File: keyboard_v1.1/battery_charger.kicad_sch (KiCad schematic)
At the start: 40 parts, among them Q3 AO3400A, Q4 AO3400A, SW13 25336NA, U1 max1737eei+T

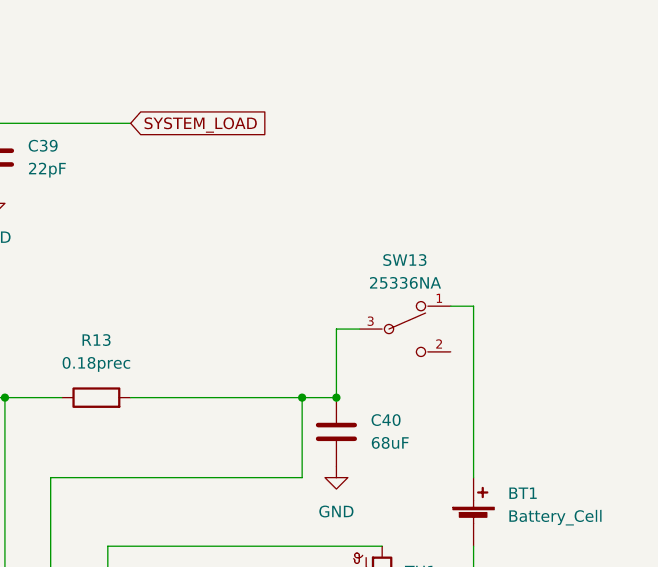
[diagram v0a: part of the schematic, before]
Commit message: 2022-04-14 added vias and led positions
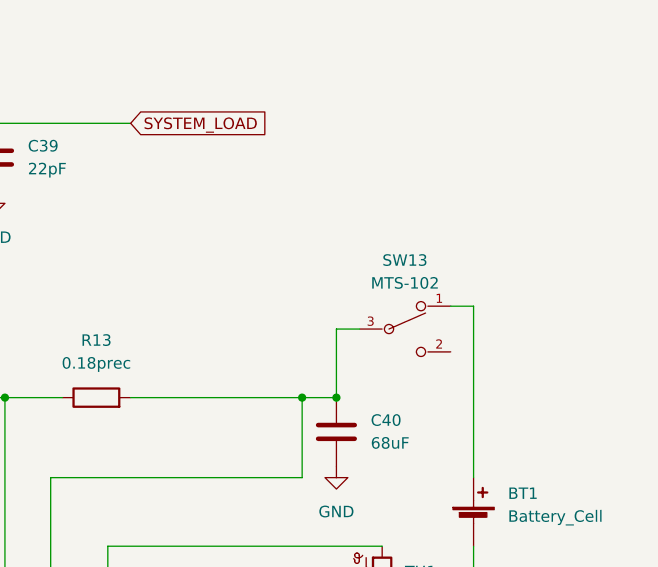
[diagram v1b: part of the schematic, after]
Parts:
- SW13: value 25336NA -> MTS-102
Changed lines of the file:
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@@
     (in_bom yes) (on_board yes) (fields_autoplaced)
     (property "Reference" "SW13" (id 0) (at 270.51 102.87 0))
-    (property "Value" "25336NA" (id 1) (at 270.51 105.41 0))
+    (property "Value" "MTS-102" (id 1) (at 270.51 105.41 0))
     (property "Footprint" "Switch_ApemInc:Apem_Inc.-25336NA-MFG" (id 2) (at 262.89 97.79 0)
       (effects (font (size 1.27 1.27)) (justify left) hide)

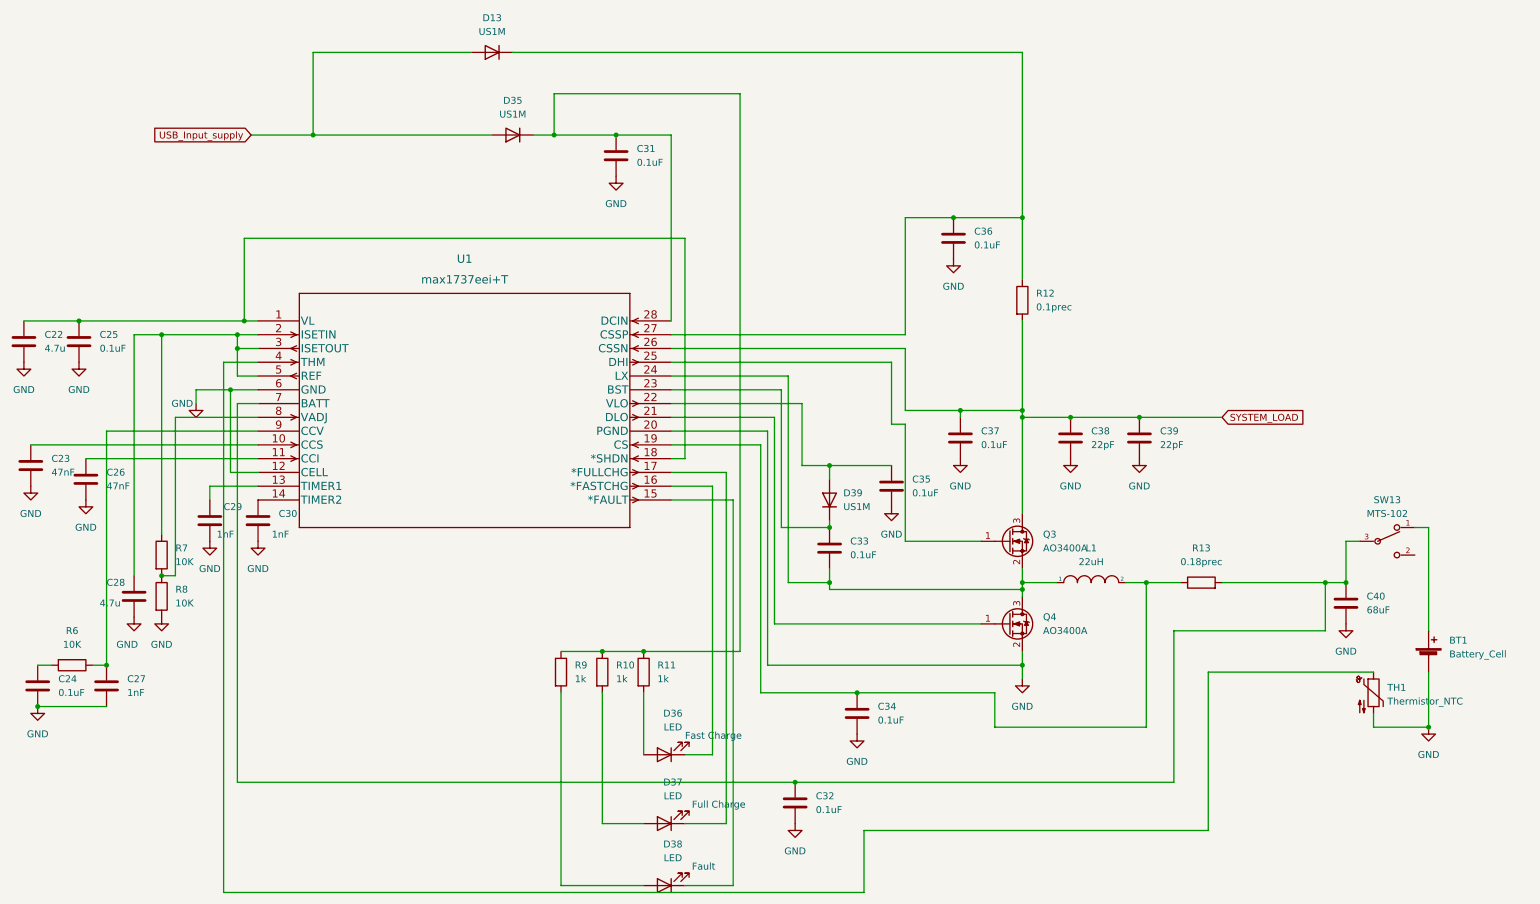
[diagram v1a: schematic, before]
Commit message: New design - schematics added (2022.07.20.)
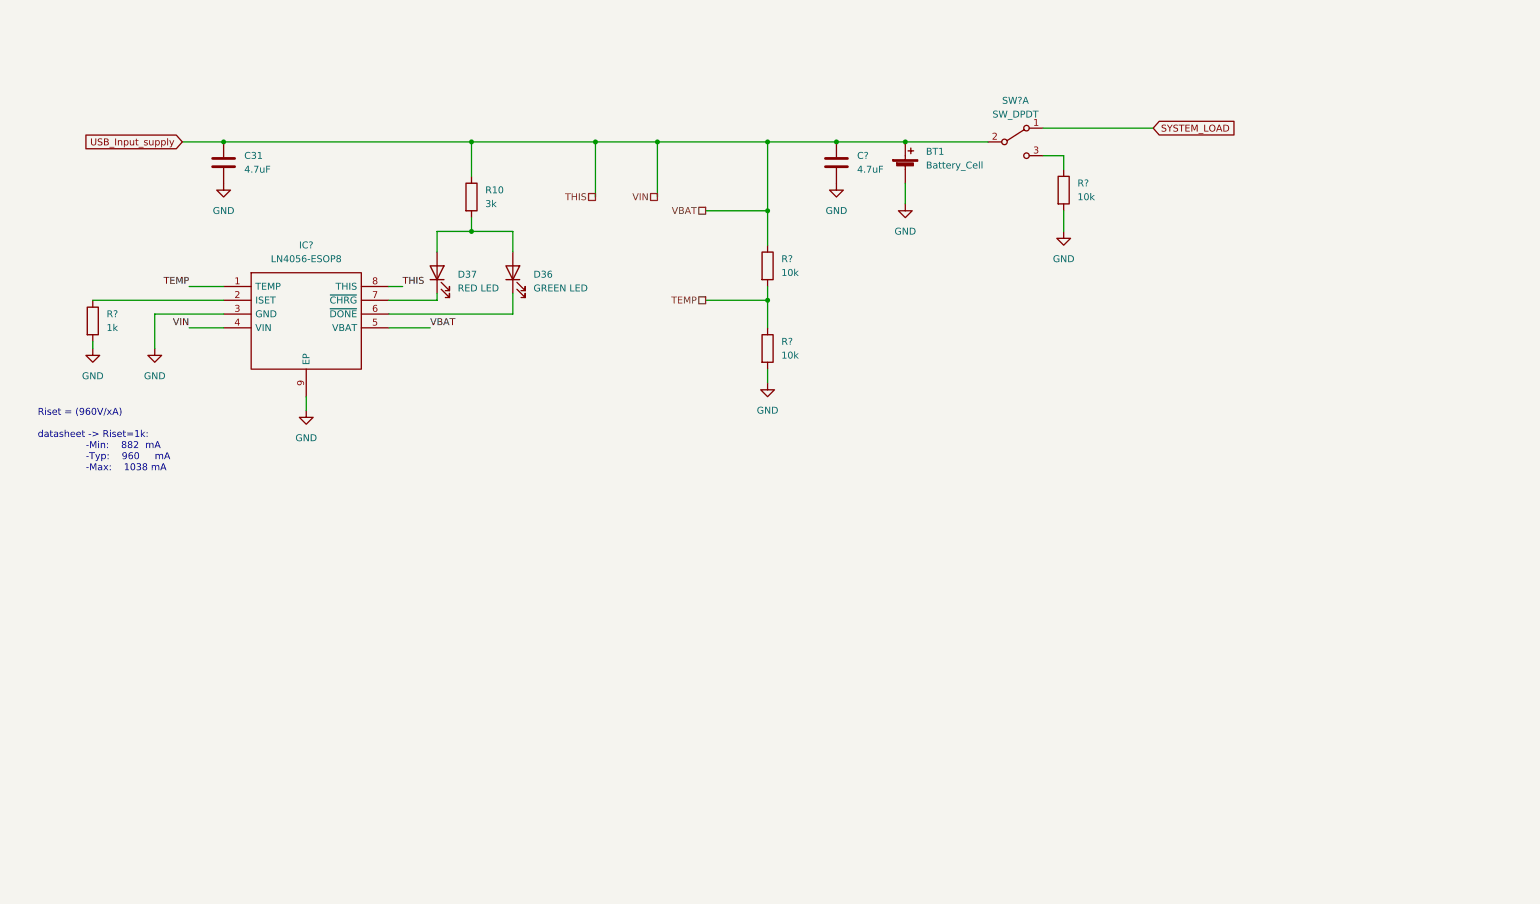
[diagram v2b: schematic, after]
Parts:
- removed C22, C28: 4.7u, Capacitor_SMD:C_0805_2012Metric_Pad1.18x1.45mm_HandSolder, symbol Device:C
- removed C23, C26: 47nF, Capacitor_SMD:C_0805_2012Metric_Pad1.18x1.45mm_HandSolder, symbol Device:C
- removed C24, C25, C32, C33, C34, C35, C36, C37: 0.1uF, Capacitor_SMD:C_0805_2012Metric_Pad1.18x1.45mm_HandSolder, symbol Device:C
- removed C27, C29, C30: 1nF, Capacitor_SMD:C_0805_2012Metric_Pad1.18x1.45mm_HandSolder, symbol Device:C
- removed C38, C39: 22pF, Capacitor_SMD:C_0805_2012Metric_Pad1.18x1.45mm_HandSolder, symbol Device:C
- removed C40: 68uF, Capacitor_THT:CP_Radial_D6.3mm_P2.50mm, symbol Device:C
- removed D13, D35, D39: US1M, Diode_SMD:D_SMA, symbol Diode:US1M
- removed D38: LED, LED_SMD:LED_0603_1608Metric_Pad1.05x0.95mm_HandSolder, symbol Device:LED
- removed L1: 22uH, inductors:inductors, symbol pspice:INDUCTOR
- removed Q3, Q4: AO3400A, Package_TO_SOT_SMD:SOT-23, symbol Transistor_FET:AO3400A
- removed R11, R9: 1k, Resistor_SMD:R_0805_2012Metric_Pad1.20x1.40mm_HandSolder, symbol Device:R
- removed R12: 0.1prec, Resistor_SMD:R_2512_6332Metric_Pad1.40x3.35mm_HandSolder, symbol Device:R
- removed R13: 0.18prec, Resistor_THT:R_Axial_DIN0309_L9.0mm_D3.2mm_P25.40mm_Horizontal, symbol Device:R
- removed R6, R7, R8: 10K, Resistor_SMD:R_0805_2012Metric_Pad1.20x1.40mm_HandSolder, symbol Device:R
- removed SW13: MTS-102, Switch_ApemInc:Apem_Inc.-25336NA-MFG, symbol Switch_ApemInc:25336NA
- removed TH1: Thermistor_NTC, Capacitor_THT:C_Disc_D5.0mm_W2.5mm_P5.00mm, symbol Device:Thermistor_NTC
- removed U1: max1737eei+T, max1737:max1737eei&plus_T, symbol max1737:max1737eei+T
- added C?: 4.7uF, Capacitor_SMD:C_0805_2012Metric_Pad1.18x1.45mm_HandSolder, symbol Device:C
- added IC?: LN4056-ESOP8, SOIC127P600X175-9N, symbol LN4056-ESOP8:LN4056-ESOP8
- added R? (x3): 10k, Resistor_SMD:R_0805_2012Metric_Pad1.20x1.40mm_HandSolder, symbol Device:R
- added R?: 1k, Resistor_SMD:R_0805_2012Metric_Pad1.20x1.40mm_HandSolder, symbol Device:R
- added SW?: SW_DPDT, symbol Switch:SW_DPDT_x2
- C31: value 0.1uF -> 4.7uF
- D36: value LED -> GREEN LED; footprint LED_SMD:LED_0603_1608Metric_Pad1.05x0.95mm_HandSolder -> LED_SMD:LED_0805_2012Metric_Pad1.15x1.40mm_HandSolder
- D37: value LED -> RED LED; footprint LED_SMD:LED_0603_1608Metric_Pad1.05x0.95mm_HandSolder -> LED_SMD:LED_0805_2012Metric_Pad1.15x1.40mm_HandSolder
- R10: value 1k -> 3k
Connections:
- net GND: now also C?.2, IC?.3 (GND), IC?.9 (EP), R?.2, R?.2, R?.2
- net SYSTEM_LOAD: now also SW?.1 (A)
- net USB_Input_supply: now also BT1.1 (+), C31.1, R10.1, C?.1, IC?.4 (VIN), IC?.5 (VBAT), IC?.8 (THIS), R?.1, SW?.2 (B)
- net at D37.2 (A), R10.2: now also D36.2 (A)
- net at D37.1 (K): now also IC?.7 (~{CHRG})
- net at D36.1 (K): now also IC?.6 (~{DONE})
- new net: IC?.2 (ISET), R?.1
- new net: R?.1, SW?.3 (C)
- new net TEMP: IC?.1 (TEMP), R?.1, R?.2
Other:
- note added: "Riset = (960V/xA) datasheet -> Riset=1k: -Min: 882 mA -Typ: 960 mA -Max: 1038 mA"
- note removed: "Fast Charge"
- note removed: "Fault"
- note removed: "Full Charge"
- moved on the sheet: BT1, C31, D36, D37, R10

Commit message: PCB layout done - 2022.07.25.
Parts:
- removed IC?: LN4056-ESOP8, SOIC127P600X175-9N, symbol LN4056-ESOP8:LN4056-ESOP8
- removed R?: 10k, Resistor_SMD:R_0805_2012Metric_Pad1.20x1.40mm_HandSolder, symbol Device:R
- added IC1: LN4056-ESOP8, SOIC127P600X175-9N, symbol LN4056-ESOP8:LN4056-ESOP8
- added R12: 10k, Resistor_SMD:R_0805_2012Metric_Pad1.20x1.40mm_HandSolder, symbol Device:R
- added TP2: TestPoint, TestPoint:TestPoint_Keystone_5010-5014_Multipurpose, symbol Connector:TestPoint
- BT1: footprint Connector_PinSocket_2.54mm:PinSocket_1x02_P2.54mm_Vertical -> Connector_PinSocket_2.54mm:PinSocket_1x02_P2.54mm_Horizontal
- SW13: renamed from SW?; footprint (none) -> Connector_PinHeader_2.54mm:PinHeader_1x03_P2.54mm_Horizontal
- gave numbers to parts that had none: 4
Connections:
- net GND: now also IC1.3 (GND), IC1.9 (EP)
- net TEMP: now also IC1.1 (TEMP), TP2.1
- net USB_Input_supply: now also IC1.4 (VIN), R12.1; no longer BT1.1 (+), C9.1, SW13.2 (B)
- net at R11.1: now also IC1.2 (ISET)
- net at D36.1 (K): now also IC1.6 (~{DONE})
- net at D37.1 (K): now also IC1.7 (~{CHRG})
- new net: BT1.1 (+), C9.1, IC1.5 (VBAT), SW13.2 (B)
- new net: IC1.8 (CE), R12.2
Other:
- moved on the sheet: BT1, C9, SW13A

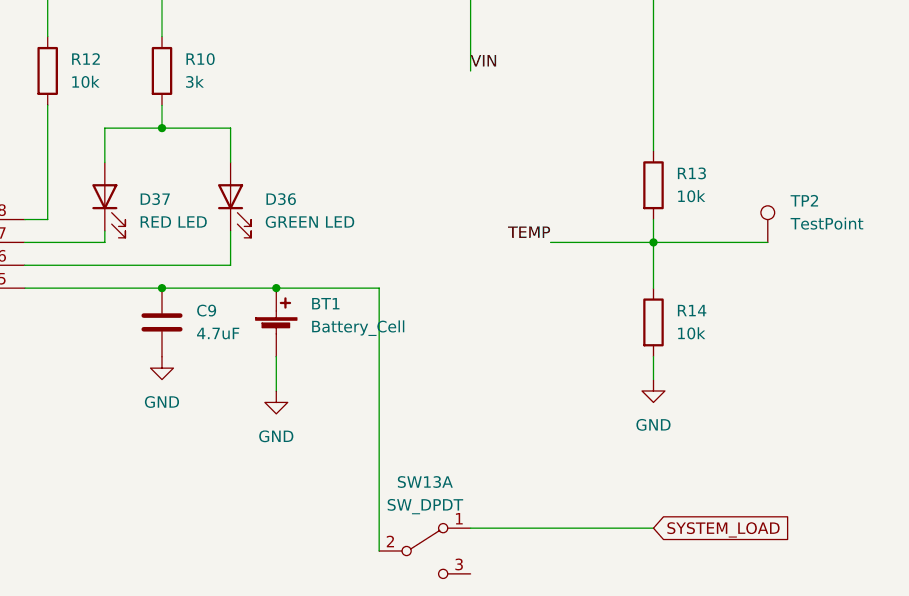
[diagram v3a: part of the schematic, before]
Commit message: Corrections on PCB design - 2022.08.04.
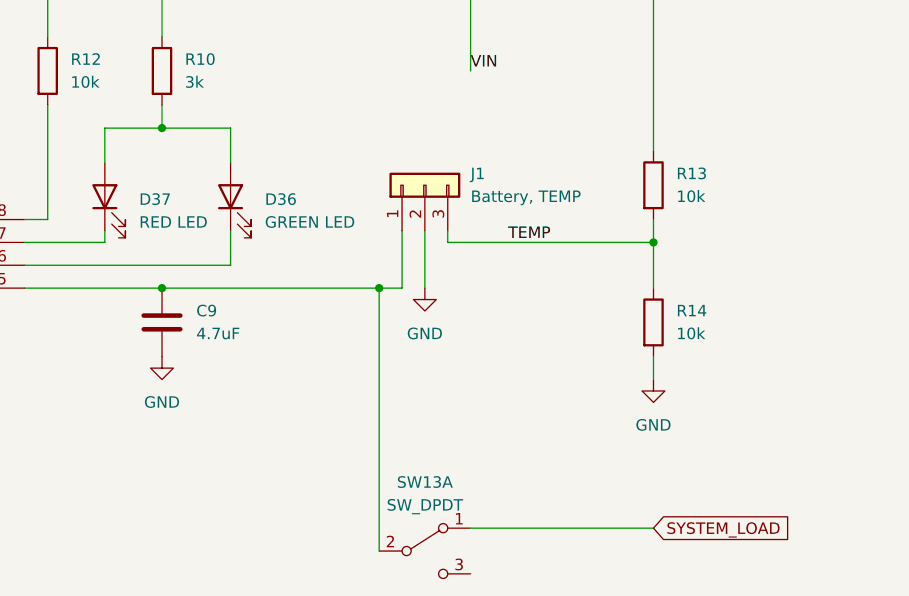
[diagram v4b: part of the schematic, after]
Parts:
- removed BT1: Battery_Cell, Connector_PinSocket_2.54mm:PinSocket_1x02_P2.54mm_Horizontal, symbol Device:Battery_Cell
- removed TP2: TestPoint, TestPoint:TestPoint_Keystone_5010-5014_Multipurpose, symbol Connector:TestPoint
- added J1: Battery, TEMP, Connector_PinSocket_2.54mm:PinSocket_1x03_P2.54mm_Horizontal, symbol Connector_Generic:Conn_01x03
- IC1: footprint SOIC127P600X175-9N -> SamacSys_Parts:SOIC127P600X175-9N
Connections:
- net GND: now also J1.2 (Pin_2)
- net TEMP: now also J1.3 (Pin_3)
- net at C9.1, IC1.5 (VBAT), SW13.2 (B): now also J1.1 (Pin_1)
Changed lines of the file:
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@@
   (junction (at 88.9 36.83) (diameter 0) (color 0 0 0 0)
   )
-  (junction (at 114.3 71.12) (diameter 0) (color 0 0 0 0)
+  (junction (at 101.6 71.12) (diameter 0) (color 0 0 0 0)
   )
   (junction (at 135.89 36.83) (diameter 0) (color 0 0 0 0)
@@
   (junction (at 101.6 53.34) (diameter 0) (color 0 0 0 0)
   )
-  (junction (at 101.6 71.12) (diameter 0) (color 0 0 0 0)
-  )
-  (wire (pts (xy 156.21 66.04) (xy 168.91 66.04))
-    (stroke (width 0) (type default) (color 0 0 0 0))
+  (junction (at 125.73 71.12) (diameter 0) (color 0 0 0 0)
   )
   (wire (pts (xy 101.6 53.34) (xy 109.22 53.34))
     (stroke (width 0) (type default) (color 0 0 0 0))
   )
-  (wire (pts (xy 144.78 66.04) (xy 156.21 66.04))
+  (wire (pts (xy 133.35 66.04) (xy 156.21 66.04))
     (stroke (width 0) (type default) (color 0 0 0 0))
   )
@@
     (stroke (width 0) (type default) (color 0 0 0 0))
   )
+  (wire (pts (xy 133.35 66.04) (xy 133.35 64.77))
+    (stroke (width 0) (type default) (color 0 0 0 0))
+  )
   (wire (pts (xy 135.89 36.83) (xy 135.89 46.99))
     (stroke (width 0) (type default) (color 0 0 0 0))
   )
-  (wire (pts (xy 125.73 71.12) (xy 114.3 71.12))
-    (stroke (width 0) (type default) (color 0 0 0 0))
-  )
   (wire (pts (xy 156.21 78.74) (xy 156.21 81.28))
     (stroke (width 0) (type default) (color 0 0 0 0))
   )
+  (wire (pts (xy 128.27 71.12) (xy 125.73 71.12))
+    (stroke (width 0) (type default) (color 0 0 0 0))
+  )
   (wire (pts (xy 95.25 53.34) (xy 101.6 53.34))
     (stroke (width 0) (type default) (color 0 0 0 0))
@@
     (stroke (width 0) (type default) (color 0 0 0 0))
   )
+  (wire (pts (xy 130.81 64.77) (xy 130.81 71.12))
+    (stroke (width 0) (type default) (color 0 0 0 0))
+  )
+  (wire (pts (xy 128.27 64.77) (xy 128.27 71.12))
+    (stroke (width 0) (type default) (color 0 0 0 0))
+  )
   (wire (pts (xy 156.21 66.04) (xy 156.21 71.12))
     (stroke (width 0) (type default) (color 0 0 0 0))
@@
     (stroke (width 0) (type default) (color 0 0 0 0))
   )
-  (wire (pts (xy 101.6 71.12) (xy 114.3 71.12))
+  (wire (pts (xy 125.73 71.12) (xy 125.73 100.33))
     (stroke (width 0) (type default) (color 0 0 0 0))
   )
@@
     (stroke (width 0) (type default) (color 0 0 0 0))
   )
-  (wire (pts (xy 125.73 100.33) (xy 125.73 71.12))
-    (stroke (width 0) (type default) (color 0 0 0 0))
-  )
   (wire (pts (xy 101.6 36.83) (xy 135.89 36.83))
     (stroke (width 0) (type default) (color 0 0 0 0))
@@
     (stroke (width 0) (type default) (color 0 0 0 0))
   )
+  (wire (pts (xy 125.73 71.12) (xy 101.6 71.12))
+    (stroke (width 0) (type default) (color 0 0 0 0))
+  )
   (wire (pts (xy 31.75 73.66) (xy 31.75 74.93))
     (stroke (width 0) (type default) (color 0 0 0 0))
@@
   )
   (wire (pts (xy 86.36 63.5) (xy 88.9 63.5))
-    (stroke (width 0) (type default) (color 0 0 0 0))
-  )
-  (wire (pts (xy 114.3 78.74) (xy 114.3 82.55))
     (stroke (width 0) (type default) (color 0 0 0 0))
   )
@@
     (property "Reference" "IC1" (id 0) (at 71.12 55.88 0))
     (property "Value" "LN4056-ESOP8" (id 1) (at 71.12 58.42 0))
-    (property "Footprint" "SOIC127P600X175-9N" (id 2) (at 114.554 55.118 0)
+    (property "Footprint" "SamacSys_Parts:SOIC127P600X175-9N" (id 2) (at 114.554 55.118 0)
       (effects (font (size 1.27 1.27)) (justify left) hide)
     )
@@
     (pin "2")
   )
-  (symbol (lib_id "power:GND") (at 114.3 82.55 0) (unit 1)
-    (in_bom yes) (on_board yes) (fields_autoplaced)
-    (property "Reference" "#PWR0119" (id 0) (at 114.3 88.9 0)
-      (effects (font (size 1.27 1.27)) hide)
-    )
-    (property "Value" "GND" (id 1) (at 114.3 87.63 0))
-    (property "Footprint" "" (id 2) (at 114.3 82.55 0)
-      (effects (font (size 1.27 1.27)) hide)
-    )
-    (property "Datasheet" "" (id 3) (at 114.3 82.55 0)
+  (symbol (lib_id "power:GND") (at 130.81 71.12 0) (unit 1)
+    (in_bom yes) (on_board yes) (fields_autoplaced)
+    (property "Reference" "#PWR0119" (id 0) (at 130.81 77.47 0)
+      (effects (font (size 1.27 1.27)) hide)
+    )
+    (property "Value" "GND" (id 1) (at 130.81 76.2 0))
+    (property "Footprint" "" (id 2) (at 130.81 71.12 0)
+      (effects (font (size 1.27 1.27)) hide)
+    )
+    (property "Datasheet" "" (id 3) (at 130.81 71.12 0)
       (effects (font (size 1.27 1.27)) hide)
     )
@@
     (pin "1")
     (pin "2")
+  )
+  (symbol (lib_id "Connector_Generic:Conn_01x03") (at 130.81 59.69 90) (unit 1)
+    (in_bom yes) (on_board yes) (fields_autoplaced)
+    (property "Reference" "J1" (id 0) (at 135.89 58.4199 90)
+      (effects (font (size 1.27 1.27)) (justify right))
+    )
+    (property "Value" "Battery, TEMP" (id 1) (at 135.89 60.9599 90)
+      (effects (font (size 1.27 1.27)) (justify right))
+    )
+    (property "Footprint" "Connector_PinSocket_2.54mm:PinSocket_1x03_P2.54mm_Horizontal" (id 2) (at 130.81 59.69 0)
+      (effects (font (size 1.27 1.27)) hide)
+    )
+    (property "Datasheet" "~" (id 3) (at 130.81 59.69 0)
+      (effects (font (size 1.27 1.27)) hide)
+    )
+    (pin "1")
+    (pin "2")
+    (pin "3")
   )
   (symbol (lib_id "power:GND") (at 101.6 78.74 0) (unit 1)
@@
     (pin "1")
   )
-  (symbol (lib_id "Device:Battery_Cell") (at 114.3 76.2 0) (unit 1)
-    (in_bom yes) (on_board yes) (fields_autoplaced)
-    (property "Reference" "BT1" (id 0) (at 118.11 72.8979 0)
-      (effects (font (size 1.27 1.27)) (justify left))
-    )
-    (property "Value" "Battery_Cell" (id 1) (at 118.11 75.4379 0)
-      (effects (font (size 1.27 1.27)) (justify left))
-    )
-    (property "Footprint" "Connector_PinSocket_2.54mm:PinSocket_1x02_P2.54mm_Horizontal" (id 2) (at 114.3 74.676 90)
-      (effects (font (size 1.27 1.27)) hide)
-    )
-    (property "Datasheet" "~" (id 3) (at 114.3 74.676 90)
-      (effects (font (size 1.27 1.27)) hide)
-    )
-    (pin "1")
-    (pin "2")
-  )
   (symbol (lib_id "power:GND") (at 156.21 81.28 0) (unit 1)
     (in_bom yes) (on_board yes) (fields_autoplaced)
@@
     (pin "2")
   )
-  (symbol (lib_id "Connector:TestPoint") (at 168.91 66.04 0) (unit 1)
-    (in_bom yes) (on_board yes) (fields_autoplaced)
-    (property "Reference" "TP2" (id 0) (at 171.45 61.4679 0)
-      (effects (font (size 1.27 1.27)) (justify left))
-    )
-    (property "Value" "TestPoint" (id 1) (at 171.45 64.0079 0)
-      (effects (font (size 1.27 1.27)) (justify left))
-    )
-    (property "Footprint" "TestPoint:TestPoint_Keystone_5010-5014_Multipurpose" (id 2) (at 173.99 66.04 0)
-      (effects (font (size 1.27 1.27)) hide)
-    )
-    (property "Datasheet" "~" (id 3) (at 173.99 66.04 0)
-      (effects (font (size 1.27 1.27)) hide)
-    )
-    (pin "1")
-  )
 )

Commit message: Firmware added
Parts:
- R11: value 1k -> 2k
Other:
- note added: "Riset = (960V/xA) datasheet -> Riset=1k: -Min: 882 mA -Typ: 960 mA -Max: 1038 mA Riset = 2.2k -> 436mA"
- note removed: "Riset = (960V/xA) datasheet -> Riset=1k: -Min: 882 mA -Typ: 960 mA -Max: 1038 mA"
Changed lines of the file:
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@@
     (stroke (width 0) (type default) (color 0 0 0 0))
   )
-  (text "Riset = (960V/xA)\n\ndatasheet -> Riset=1k:\n				-Min:	882  mA \n				-Typ:	960	 mA	\n				-Max:	1038 mA"
+  (text "Riset = (960V/xA)\n\ndatasheet -> Riset=1k:\n				-Min:	882  mA \n				-Typ:	960	 mA	\n				-Max:	1038 mA\n\nRiset = 2.2k -> 436mA"
     (at 21.59 97.79 0)
     (effects (font (size 1.27 1.27)) (justify left bottom))
@@
       (effects (font (size 1.27 1.27)) (justify left))
     )
-    (property "Value" "1k" (id 1) (at 34.29 71.1199 0)
-      (effects (font (size 1.27 1.27)) (justify left))
-    )
+    (property "Value" "2k" (id 1) (at 34.29 71.1199 0)
+      (effects (font (size 1.27 1.27)) (justify left))
+    )
